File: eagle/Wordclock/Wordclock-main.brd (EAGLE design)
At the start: 50 x 50 mm, 36 parts, among them IC1 MEGA8-P, J1 AVR_SPI_PRG_6PTH, Q1 16MHz

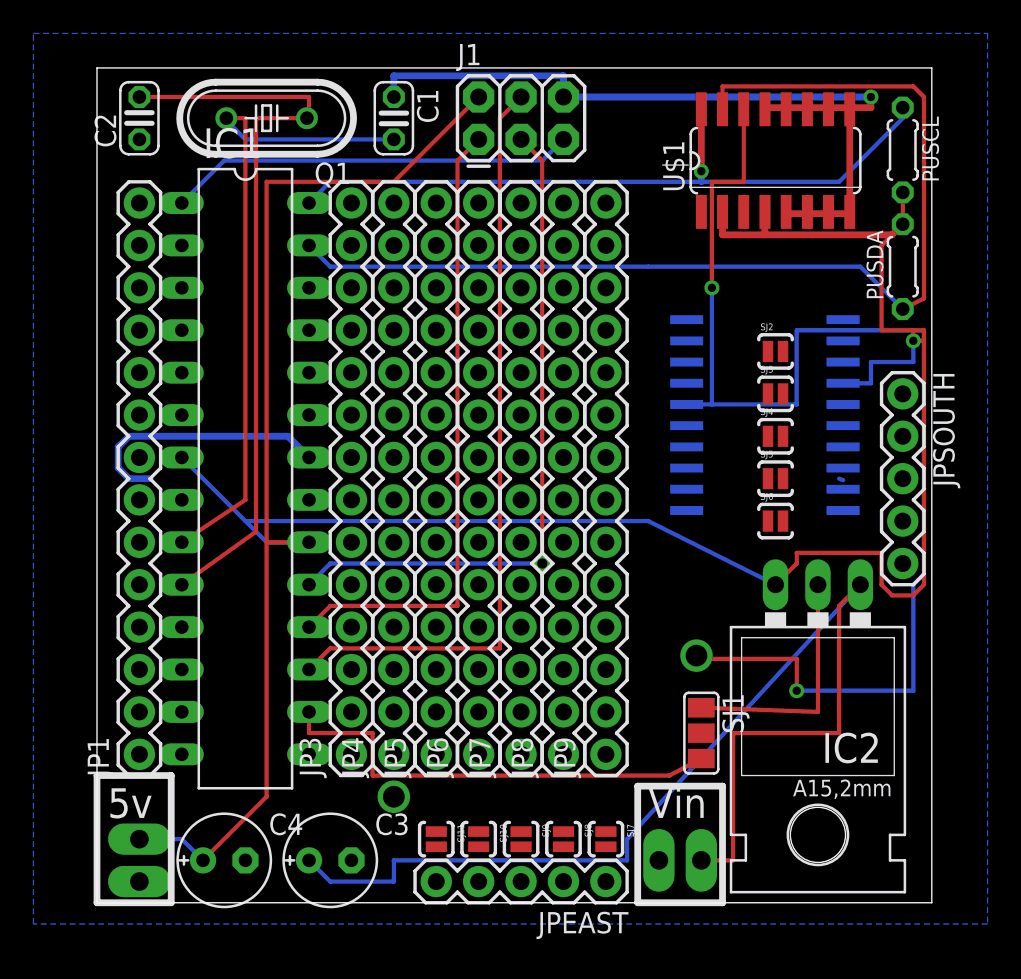
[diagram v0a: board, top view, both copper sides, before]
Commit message: wired the south connector, still east to do.
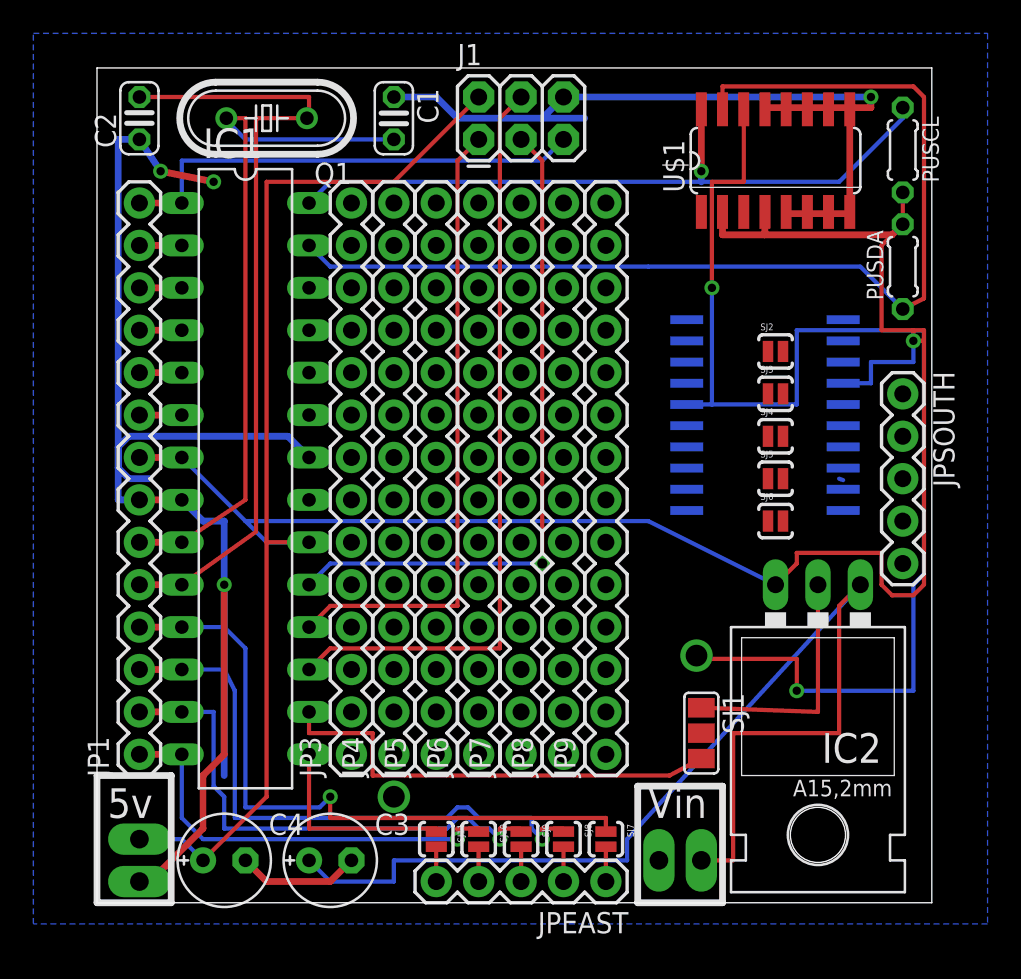
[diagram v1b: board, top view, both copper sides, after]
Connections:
- net GND: now also JP1.7
- net N$20: now also JP1.13
- net N$21: now also JP1.12
- net N$22: now also JP1.11
- net N$23: now also JP1.10
- net N$24: now also JP1.9
- net N$26: now also JP1.1
- net N$27: now also JP1.2
- net N$28: now also JP1.3
- net N$29: now also JP1.4
- net N$4: now also JP1.6
- net N$5: now also JP1.5
- net RESET: now also JP1.14
- net VCC: now also JP1.8
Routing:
- net GND: track 78.8 -> 158.0 mm, vias 1 -> 4
- net N$29: track 0.00 -> 40.2 mm, vias 0 -> 1
- net N$28: track 0.00 -> 35.9 mm, vias 0 -> 1
- net N$27: track 0.00 -> 30.9 mm, vias 0 -> 1
- net N$26: track 0.00 -> 25.3 mm, vias 0 -> 1
- net N$25: track 0.00 -> 12.1 mm
- net RESET: track 24.4 -> 28.5 mm
- net N$24: track 0.00 -> 2.54 mm
- net N$23: track 0.00 -> 2.54 mm
- net N$22: track 0.00 -> 2.54 mm
- net N$21: track 0.00 -> 2.54 mm
- net N$20: track 0.00 -> 2.54 mm
- net N$5: track 44.8 -> 47.4 mm
- net N$4: track 39.4 -> 41.9 mm
- net VCC: track 166.3 -> 168.8 mm
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
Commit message: nearly finished, 1 problem of overlap with battery + pin at the check rule step.
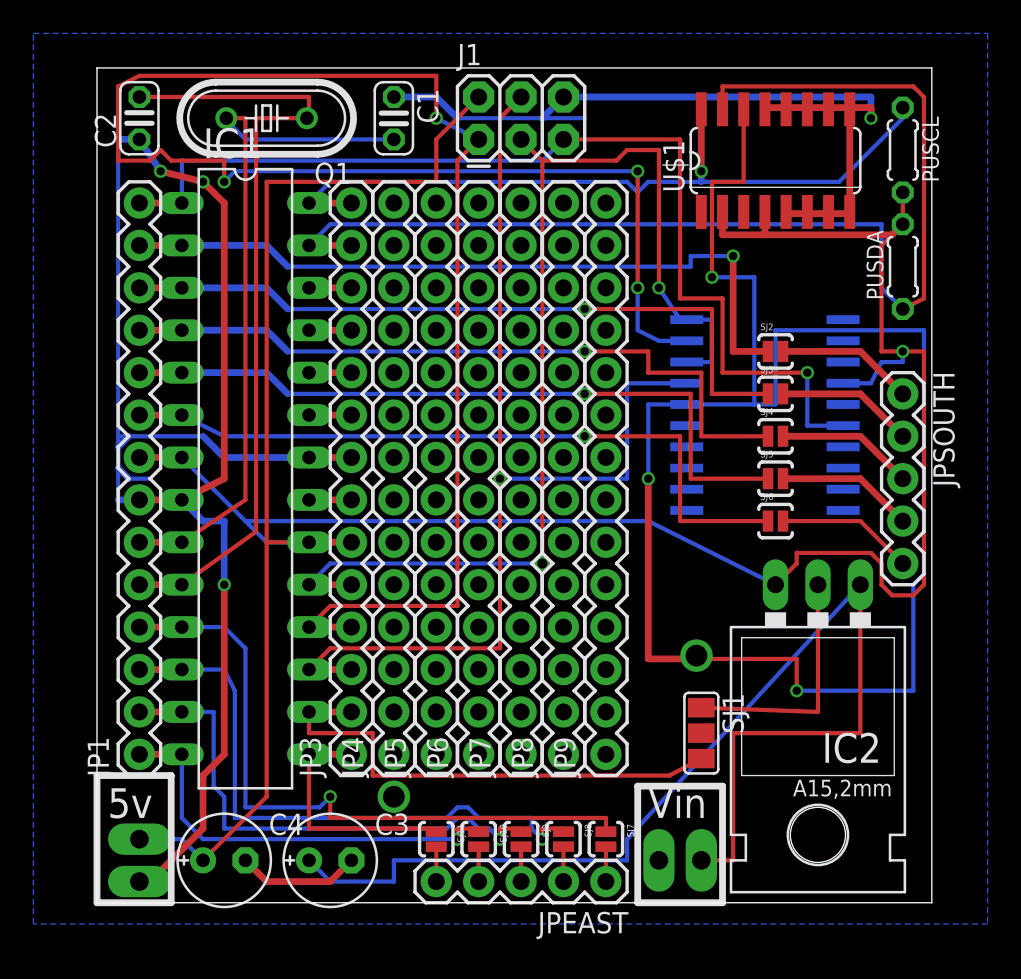
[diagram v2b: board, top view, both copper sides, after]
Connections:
- new net S$2: IC1.26, JP3.12
- new net S$3: IC1.25, JP3.11
- new net S$4: IC1.24, JP3.10
- new net S$5: IC1.23, JP3.9
- new net S$6: IC1.21, JP3.7
- net GND: now also JP3.8
- net N$12: now also JP3.5
- net N$13: now also JP3.4
- net N$14: now also JP3.3
- net N$25: now also JP3.1
- net N$30: now also JP3.14
- net N$31: now also JP3.13
- net N$6: now also JP3.2
- net VCC: now also JP3.6
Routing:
- net N$13: track 37.9 -> 115.5 mm, vias 0 -> 4
- net N$20: track 2.54 -> 44.3 mm, vias 0 -> 1
- net N$23: track 2.54 -> 43.1 mm, vias 0 -> 1
- net N$22: track 2.54 -> 43.1 mm, vias 0 -> 1
- net N$21: track 2.54 -> 43.1 mm, vias 0 -> 1
- net N$24: track 2.54 -> 42.8 mm, vias 0 -> 1
- net RESET: track 28.5 -> 62.1 mm, vias 0 -> 1
- net N$12: track 40.4 -> 66.5 mm, vias 1 -> 2
- net N$7: track 74.6 -> 98.1 mm, vias 2 -> 3
- net N$14: track 45.5 -> 64.6 mm, vias 0 -> 1
- net GND: track 158.0 -> 171.5 mm
- net N$17: track 0.00 -> 8.04 mm
- net N$15: track 0.00 -> 8.04 mm
- net N$19: track 0.00 -> 8.04 mm
- net N$18: track 0.00 -> 8.04 mm
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
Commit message: v1.0 : no fixing holes.
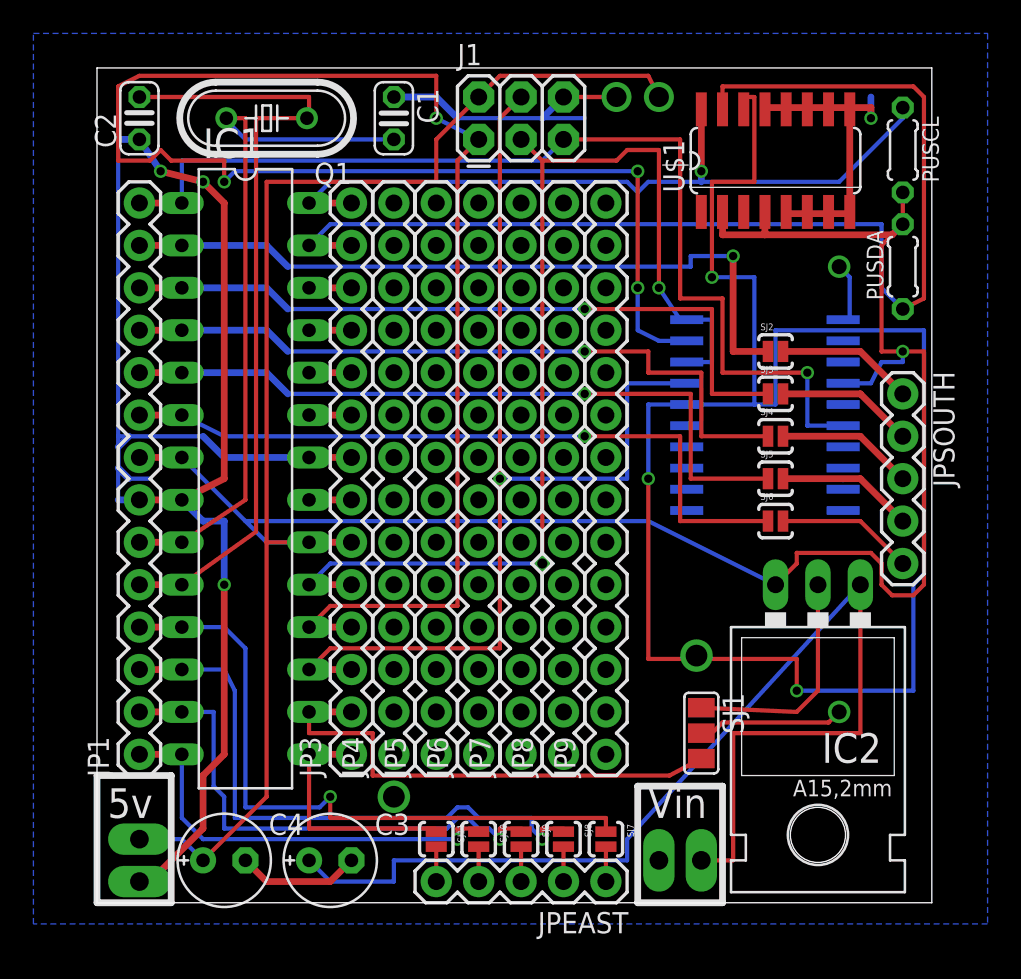
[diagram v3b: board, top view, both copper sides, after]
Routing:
- net GND: track 171.5 -> 155.6 mm, vias 4 -> 5
- net VCC: track 169.4 -> 181.5 mm, vias 1 -> 2
- net N$2: track 0.00 -> 8.78 mm, vias 0 -> 1
- net S$1: track 0.00 -> 3.44 mm, vias 0 -> 1
- net N$7: track 98.1 -> 100.0 mm
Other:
- board text added: "+"
- board text added: "-"
- board text added: "- +"
- board text added: "100uF"
- board text added: "10k+"
- board text added: "10uF"
- board text added: "ATmega328"
- board text added: "CR2320"
- board text added: "DS3231"
- board text added: "LM7805"
- board text added: "Main board"
- board text added: "Order #xxxxxxx"
- board text added: "http://kalshagar.wikispaces.com/WordClock"
- board text added: "v1.0 (Jan2012)"
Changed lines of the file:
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@@
 <layer number="102" name="Vscore" color="7" fill="1" visible="no" active="yes"/>
 <layer number="103" name="tMap" color="7" fill="1" visible="no" active="yes"/>
-<layer number="104" name="Name" color="16" fill="1" visible="no" active="yes"/>
+<layer number="104" name="Name" color="16" fill="1" visible="yes" active="yes"/>
 <layer number="105" name="tPlate" color="7" fill="1" visible="no" active="yes"/>
 <layer number="106" name="bPlate" color="7" fill="1" visible="no" active="yes"/>
@@
 <wire x1="37.465" y1="6.985" x2="37.465" y2="0" width="0.4064" layer="21"/>
 <wire x1="37.465" y1="0" x2="32.385" y2="0" width="0.4064" layer="21"/>
+<text x="36.195" y="45.085" size="0.8128" layer="104">DS3231</text>
+<text x="40.64" y="8.89" size="0.8128" layer="104">LM7805</text>
+<text x="30.48" y="46.355" size="0.8128" layer="104">-   +</text>
+<text x="27.94" y="6.35" size="0.8128" layer="26" rot="MR0">CR2320</text>
+<text x="8.255" y="7.62" size="1.27" layer="104" rot="R90">ATmega328</text>
+<text x="0.635" y="23.495" size="0.8128" layer="104">-</text>
+<text x="0.635" y="26.035" size="0.8128" layer="104">+</text>
+<text x="13.335" y="22.225" size="0.8128" layer="104">+</text>
+<text x="13.335" y="27.305" size="0.8128" layer="104">-</text>
+<text x="0.635" y="1.905" size="0.8128" layer="104">-</text>
+<text x="0.635" y="4.445" size="0.8128" layer="104">+</text>
+<text x="34.29" y="3.81" size="0.8128" layer="104">-</text>
+<text x="34.925" y="0.635" size="0.8128" layer="104">+</text>
+<text x="48.895" y="43.815" size="0.8128" layer="104" rot="R90">10k+</text>
+<text x="48.895" y="36.83" size="0.8128" layer="104" rot="R90">10k+</text>
+<text x="12.7" y="0.635" size="0.6096" layer="104">100uF</text>
+<text x="6.35" y="0.635" size="0.6096" layer="104">10uF</text>
+<wire x1="44.45" y1="37.465" x2="44.45" y2="12.7" width="0.254" layer="104" style="dashdot"/>
+<rectangle x1="13.97" y1="7.62" x2="16.51" y2="43.18" layer="104"/>
+<rectangle x1="1.27" y1="8.255" x2="3.81" y2="43.18" layer="104"/>
+<rectangle x1="21.59" y1="44.45" x2="24.13" y2="46.99" layer="104"/>
+<text x="9.525" y="1.905" size="0.8128" layer="104">-</text>
+<text x="15.875" y="1.905" size="0.8128" layer="104">-</text>
+<wire x1="33.655" y1="19.05" x2="36.195" y2="23.495" width="0.4064" layer="104"/>
+<wire x1="36.195" y1="23.495" x2="36.195" y2="19.685" width="0.4064" layer="104"/>
+<wire x1="36.195" y1="19.685" x2="36.195" y2="16.51" width="0.4064" layer="104"/>
+<wire x1="36.195" y1="16.51" x2="38.735" y2="21.59" width="0.4064" layer="104"/>
+<wire x1="34.925" y1="19.685" x2="36.195" y2="19.685" width="0.4064" layer="104"/>
+<text x="10.16" y="15.24" size="0.8128" layer="104" rot="R90">http://kalshagar.wikispaces.com/WordClock</text>
+<text x="49.53" y="1.905" size="1.27" layer="104" rot="R90">Order #xxxxxxx</text>
+<text x="7.62" y="33.02" size="0.8128" layer="104" rot="R90">v1.0 (Jan2012)</text>
+<text x="7.62" y="24.13" size="0.8128" layer="104" rot="R90">Main board</text>
 </plain>
 <attributes>
@@
 <vertex x="-3.81" y="-1.27"/>
 </polygon>
-<wire x1="43.18" y1="19.05" x2="43.18" y2="11.43" width="0.254" layer="1"/>
-<wire x1="43.18" y1="11.43" x2="36.195" y2="11.684" width="0.254" layer="1"/>
+<wire x1="43.18" y1="19.05" x2="43.18" y2="12.7" width="0.254" layer="1"/>
+<wire x1="43.18" y1="12.7" x2="41.91" y2="11.43" width="0.254" layer="1"/>
+<wire x1="41.91" y1="11.43" x2="36.195" y2="11.684" width="0.254" layer="1"/>
 <wire x1="44.45" y1="25.4" x2="44.6900125" y2="25.3128" width="0.254" layer="16"/>
 <wire x1="1.905" y1="27.94" x2="1.27" y2="27.305" width="0.4064" layer="16"/>
@@
 <wire x1="45.085" y1="47.625" x2="46.355" y2="47.625" width="0.4064" layer="1"/>
 <wire x1="46.355" y1="47.625" x2="46.355" y2="46.99" width="0.4064" layer="1"/>
-<wire x1="27.94" y1="48.26" x2="46.355" y2="48.26" width="0.4064" layer="16"/>
 <wire x1="46.355" y1="48.26" x2="46.355" y2="46.99" width="0.4064" layer="16"/>
 <wire x1="41.275" y1="41.275" x2="45.085" y2="41.275" width="0.4064" layer="1"/>
@@
 <wire x1="7.62" y1="25.4" x2="7.62" y2="41.91" width="0.4064" layer="1"/>
 <wire x1="7.62" y1="41.91" x2="6.35" y2="43.18" width="0.4064" layer="1"/>
+<via x="31.115" y="48.26" extent="1-16" drill="1.2" shape="octagon"/>
+<wire x1="27.94" y1="48.26" x2="31.115" y2="48.26" width="0.254" layer="1"/>
 <wire x1="45.085" y1="47.625" x2="45.085" y2="47.5234" width="0" layer="19" extent="1-1"/>
 <wire x1="40.005" y1="47.5234" x2="40.005" y2="47.625" width="0" layer="19" extent="1-1"/>
@@
 <contactref element="DS3234" pad="1"/>
 <contactref element="SJ1" pad="2"/>
-<wire x1="36.195" y1="10.16" x2="44.69" y2="34.925" width="0" layer="19" extent="1-16"/>
+<wire x1="36.195" y1="10.16" x2="36.83" y2="10.16" width="0.254" layer="1"/>
+<wire x1="36.83" y1="10.16" x2="37.465" y2="10.795" width="0.254" layer="1"/>
+<wire x1="37.465" y1="10.795" x2="43.815" y2="10.795" width="0.254" layer="1"/>
+<via x="44.45" y="11.43" extent="1-16" drill="0.9" shape="octagon"/>
+<wire x1="43.815" y1="10.795" x2="44.45" y2="11.43" width="0.254" layer="1"/>
+<wire x1="44.45" y1="11.43" x2="44.69" y2="34.925" width="0" layer="19" extent="16-16"/>
 </signal>
 <signal name="RESET">
@@
 <wire x1="46.99" y1="33.02" x2="48.26" y2="33.02" width="0.254" layer="1"/>
 <wire x1="49.53" y1="33.02" x2="48.26" y2="33.02" width="0.254" layer="1"/>
+<wire x1="22.86" y1="48.26" x2="24.13" y2="49.53" width="0.254" layer="1"/>
+<wire x1="24.13" y1="49.53" x2="33.02" y2="49.53" width="0.254" layer="1"/>
+<via x="33.655" y="48.26" extent="1-16" drill="1.2" shape="octagon"/>
+<wire x1="33.02" y1="49.53" x2="33.655" y2="48.26" width="0.254" layer="1"/>
 <wire x1="40.005" y1="41.275" x2="40.005" y2="41.3766" width="0" layer="19" extent="1-1"/>
 <wire x1="37.465" y1="41.3766" x2="37.465" y2="41.275" width="0" layer="19" extent="1-1"/>
@@
 <wire x1="39.37" y1="37.465" x2="36.83" y2="37.465" width="0.254" layer="16"/>
 <wire x1="36.83" y1="37.465" x2="36.83" y2="43.18" width="0.254" layer="1"/>
-<wire x1="36.83" y1="43.18" x2="38.735" y2="43.18" width="0.254" layer="1"/>
-<wire x1="38.735" y1="43.18" x2="38.735" y2="47.625" width="0.254" layer="1"/>
+<wire x1="36.83" y1="43.18" x2="39.37" y2="43.18" width="0.254" layer="1"/>
+<wire x1="39.37" y1="43.18" x2="39.37" y2="48.26" width="0.254" layer="1"/>
 <wire x1="41.91" y1="12.7" x2="41.91" y2="14.605" width="0.254" layer="1"/>
-<wire x1="41.91" y1="14.605" x2="36.195" y2="14.605" width="0.254" layer="1"/>
-<wire x1="36.195" y1="14.605" x2="33.02" y2="14.605" width="0.4064" layer="1"/>
-<wire x1="33.02" y1="14.605" x2="33.02" y2="25.4" width="0.4064" layer="1"/>
+<wire x1="41.91" y1="14.605" x2="33.02" y2="14.605" width="0.254" layer="1"/>
+<wire x1="33.02" y1="14.605" x2="33.02" y2="25.4" width="0.254" layer="1"/>
 <via x="33.02" y="25.4" extent="1-16" drill="0.5" shape="octagon"/>
 <wire x1="33.02" y1="25.4" x2="33.02" y2="29.845" width="0.254" layer="16"/>
 <wire x1="39.37" y1="29.845" x2="33.02" y2="29.845" width="0.254" layer="16"/>
+<wire x1="39.37" y1="48.26" x2="38.735" y2="48.26" width="0.254" layer="1"/>
 </signal>
 <signal name="S$2">
@@
 <wire x1="12.7" y1="24.13" x2="15.24" y2="24.13" width="0.4064" layer="1"/>
 </signal>
+<signal name="S$1">
+<via x="44.45" y="38.1" extent="1-16" drill="0.9" shape="octagon"/>
+<wire x1="45.085" y1="34.925" x2="45.085" y2="37.465" width="0.254" layer="16"/>
+<wire x1="45.085" y1="37.465" x2="44.45" y2="38.1" width="0.254" layer="16"/>
+</signal>
 </signals>
